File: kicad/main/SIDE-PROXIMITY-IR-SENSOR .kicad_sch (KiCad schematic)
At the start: 4 parts

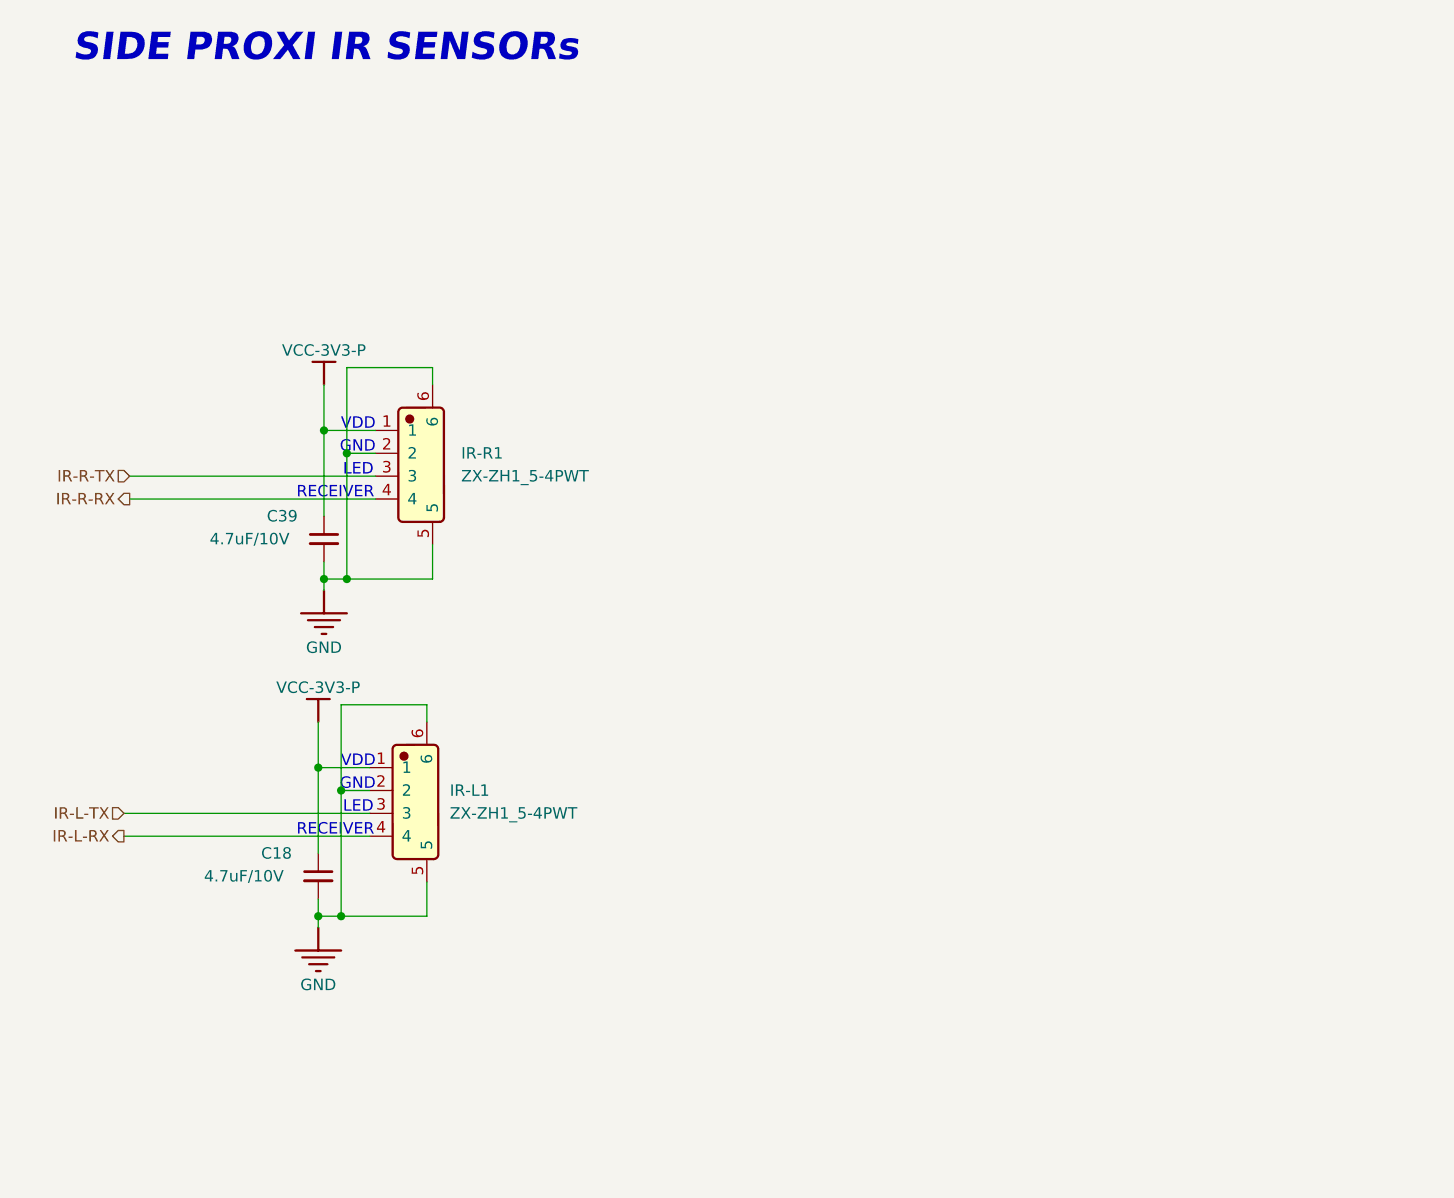
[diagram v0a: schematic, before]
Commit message: Side sensor VL6180
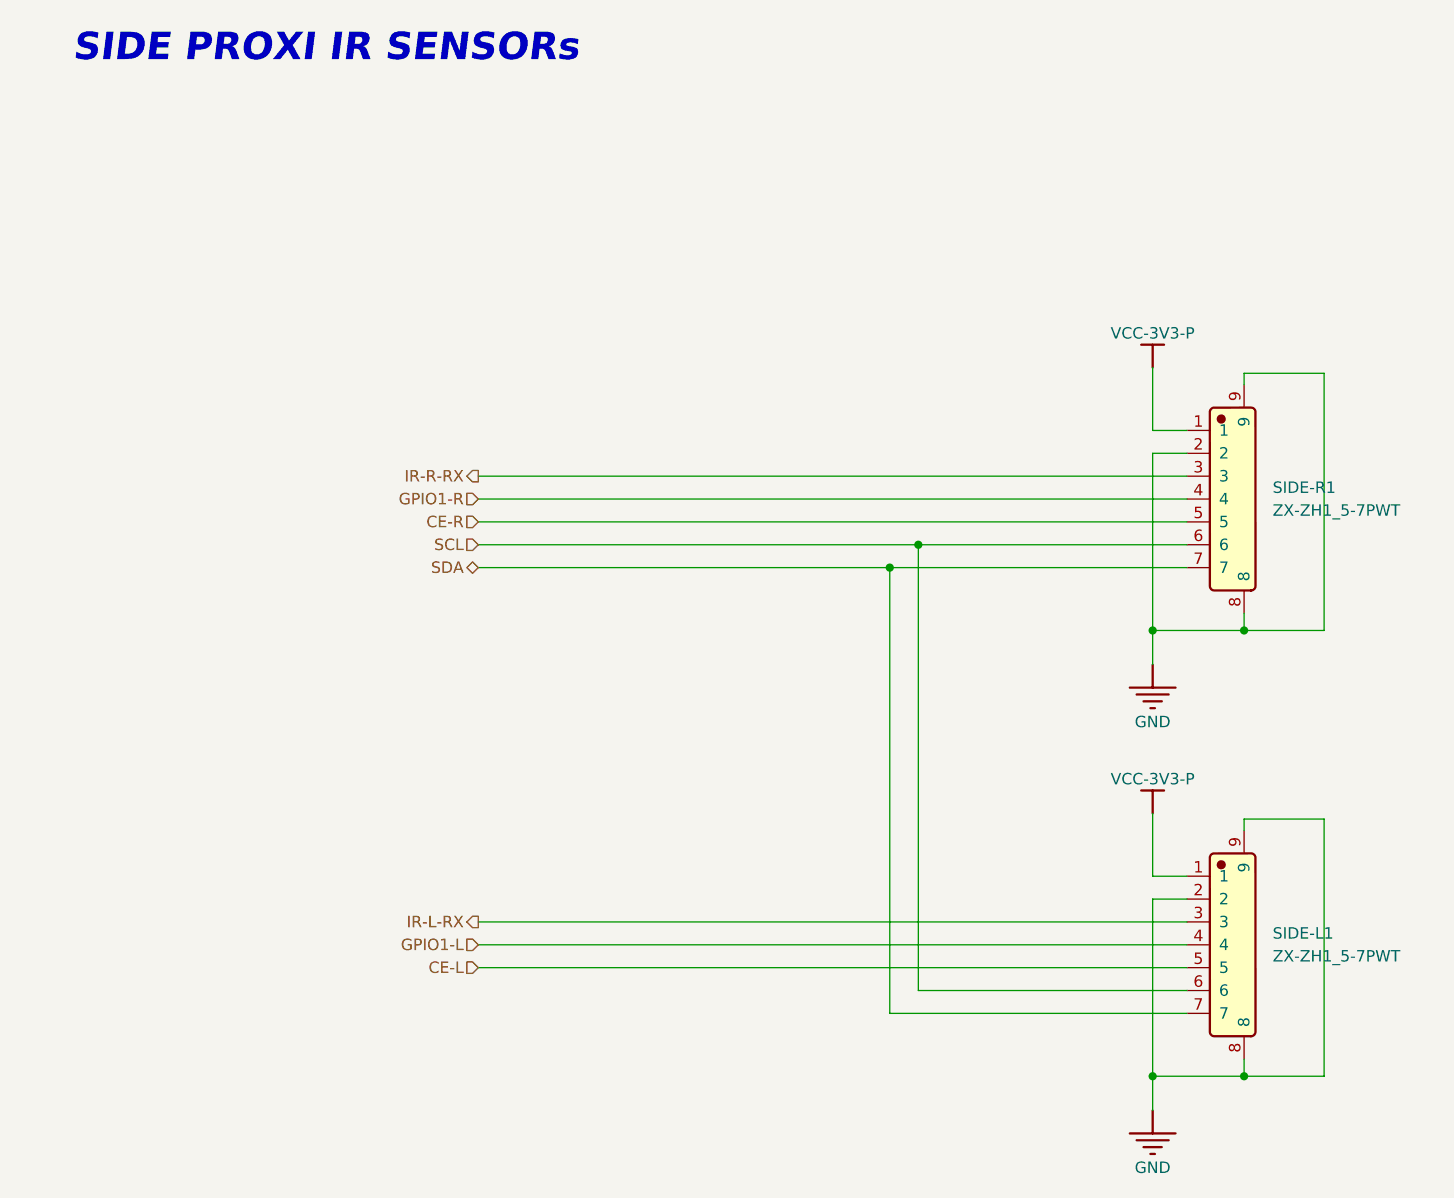
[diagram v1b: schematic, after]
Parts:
- removed C18, C39: 4.7uF/10V, symbol Device:C_Small
- removed IR-L1, IR-R1: ZX-ZH1_5-4PWT, JLCImport:ZX-ZH1_5-4PWT, symbol JLCImport:ZX-ZH1_5-4PWT
- added SIDE-L1, SIDE-R1: ZX-ZH1_5-7PWT, JLCImport:ZX-ZH1_5-7PWT, symbol JLCImport:ZX-ZH1_5-7PWT
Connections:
- net GND: now also SIDE-L1.2, SIDE-L1.8, SIDE-L1.9, SIDE-R1.2, SIDE-R1.8, SIDE-R1.9
- net IR-L-RX: now also SIDE-L1.3
- net IR-R-RX: now also SIDE-R1.3
- net VCC-3V3-P: now also SIDE-L1.1, SIDE-R1.1
- new net CE-L: SIDE-L1.5
- new net CE-R: SIDE-R1.5
- new net GPIO1-L: SIDE-L1.4
- new net GPIO1-R: SIDE-R1.4
- new net SCL: SIDE-L1.6, SIDE-R1.6
- new net SDA: SIDE-L1.7, SIDE-R1.7
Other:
- note removed: "GND"
- note removed: "LED"
- note removed: "RECEIVER"
- note removed: "VDD"
